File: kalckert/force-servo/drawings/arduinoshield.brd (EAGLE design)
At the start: 100 x 80 mm, 24 parts, among them IC1 MCP604P, IC3 7806T

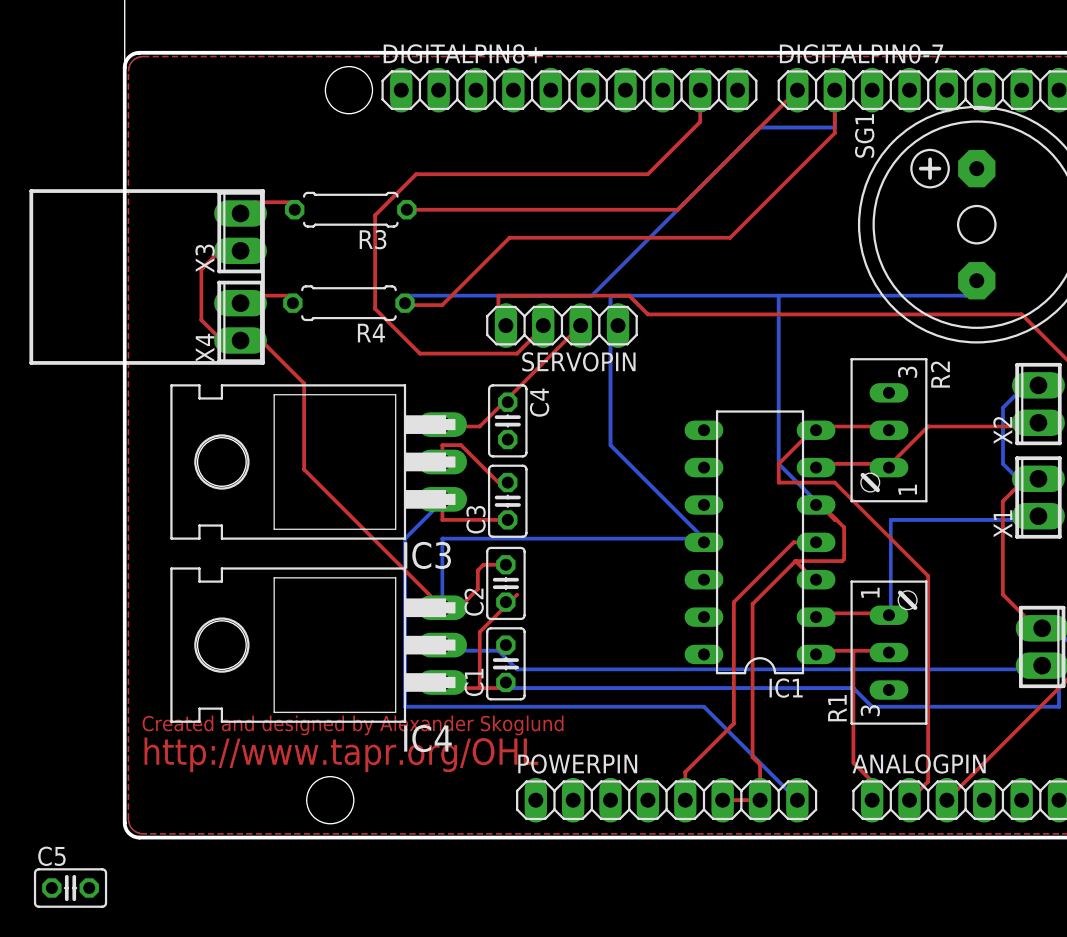
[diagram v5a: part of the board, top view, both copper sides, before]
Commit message: Added a calibration sequence in the arduino program.
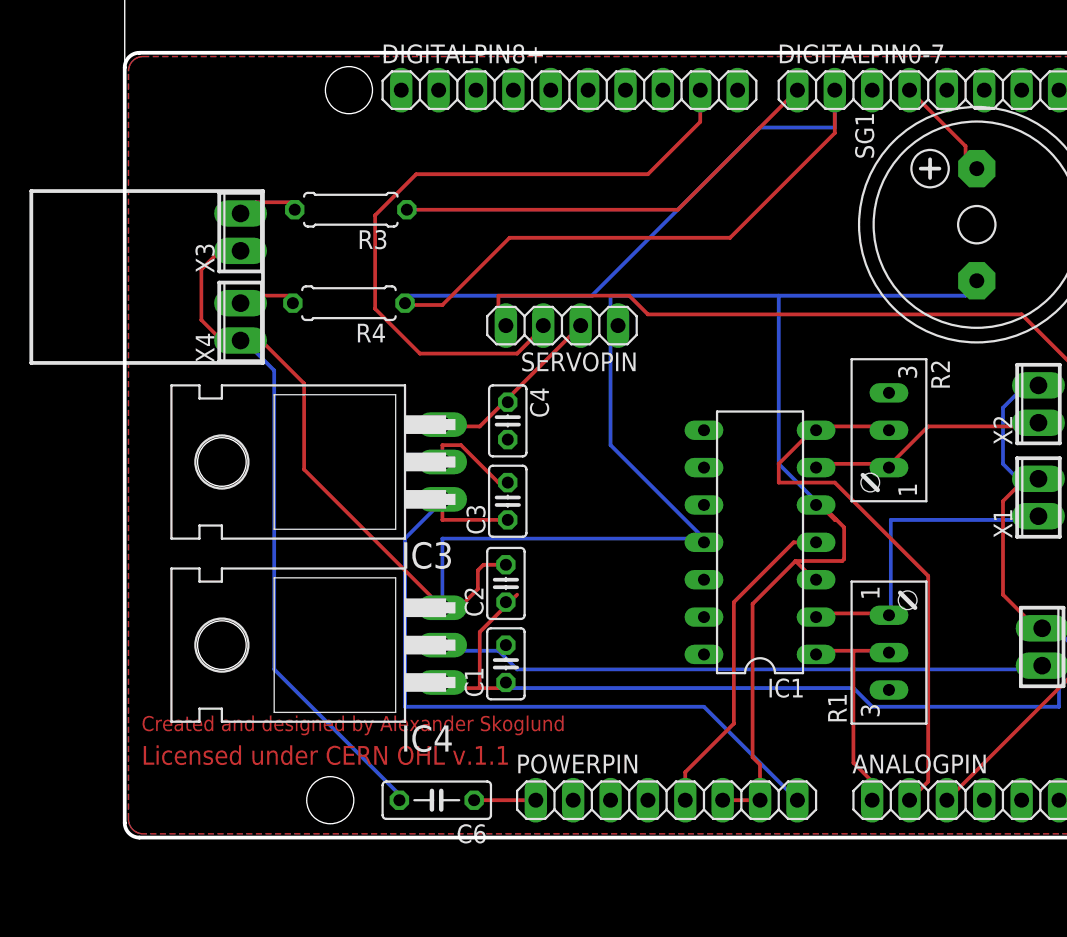
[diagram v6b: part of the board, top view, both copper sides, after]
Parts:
- removed C5: 10uF, resistor:C025-025X050
- added C6: 10uF, resistor:C050-025X075
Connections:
- net GND: now also C6.2; no longer C5.2
- net RESET: now also C6.1; no longer C5.1
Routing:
- net GND: track 156.7 -> 193.0 mm
- net BUZZER: track 0.00 -> 7.46 mm
- net RESET: track 0.00 -> 4.19 mm
- net N$3: track 6.13 -> 6.77 mm
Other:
- board text added: "Licensed under CERN OHL v.1.1"
- board text removed: "http://www.tapr.org/OHL"
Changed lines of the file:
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@@
 <wire x1="9.398" y1="32.258" x2="-6.35" y2="32.258" width="0.254" layer="21"/>
 <wire x1="-6.35" y1="32.258" x2="-6.35" y2="43.942" width="0.254" layer="21"/>
-<text x="1.143" y="4.953" size="1.778" layer="1">http://www.tapr.org/OHL</text>
+<text x="1.143" y="4.953" size="1.27" layer="1">Licensed under CERN OHL v.1.1</text>
 <text x="1.143" y="7.239" size="1.016" layer="1">Created and designed by Alexander Skoglund</text>
 </plain>
@@
 <attribute name="OC_FARNELL" value="unknown" x="80.137" y="59.69" size="1.778" layer="27" rot="R90" display="off"/>
 </element>
-<element name="C5" library="resistor" package="C025-025X050" value="10uF" x="-3.683" y="-3.429"/>
+<element name="C6" library="resistor" package="C050-025X075" value="10uF" x="21.209" y="2.54" rot="R180"/>
 </elements>
 <signals>
@@
 <wire x1="39.37" y1="20.32" x2="39.37" y2="20.066" width="0.254" layer="16"/>
 <wire x1="21.59" y1="15.24" x2="21.59" y2="15.621" width="0.254" layer="16"/>
-<contactref element="C5" pad="2"/>
-<wire x1="-2.413" y1="-3.429" x2="21.59" y2="15.24" width="0" layer="19" extent="16-16"/>
+<contactref element="C6" pad="2"/>
+<wire x1="10.16" y1="11.43" x2="19.05" y2="2.54" width="0.254" layer="16"/>
+<wire x1="10.16" y1="31.75" x2="10.16" y2="11.43" width="0.254" layer="16"/>
+<wire x1="8.89" y1="33.02" x2="10.16" y2="31.75" width="0.254" layer="16"/>
+<wire x1="19.05" y1="2.54" x2="18.669" y2="2.54" width="0.254" layer="16"/>
+<wire x1="8.89" y1="33.02" x2="7.874" y2="33.782" width="0.254" layer="16"/>
 </signal>
 <signal name="VCCSERVO">
@@
 <contactref element="SG1" pad="+"/>
 <contactref element="DIGITALPIN0-7" pad="4"/>
-<wire x1="57.912" y1="45.466" x2="53.34" y2="50.8" width="0" layer="19" extent="1-1"/>
+<wire x1="57.15" y1="46.99" x2="53.34" y2="50.8" width="0.254" layer="1"/>
+<wire x1="57.15" y1="45.72" x2="57.15" y2="46.99" width="0.254" layer="1"/>
+<wire x1="57.15" y1="45.72" x2="57.912" y2="45.466" width="0.254" layer="1"/>
 </signal>
 <signal name="VIN">
@@
 <wire x1="39.37" y1="8.89" x2="45.72" y2="2.54" width="0.254" layer="16"/>
 <wire x1="19.05" y1="8.89" x2="39.37" y2="8.89" width="0.254" layer="16"/>
-<wire x1="19.05" y1="20.32" x2="19.05" y2="8.89" width="0.254" layer="16"/>
 <wire x1="21.59" y1="22.86" x2="19.05" y2="20.32" width="0.254" layer="16"/>
 <wire x1="21.59" y1="22.86" x2="21.59" y2="22.987" width="0.254" layer="16"/>
+<wire x1="19.05" y1="8.89" x2="19.05" y2="20.32" width="0.254" layer="16"/>
 </signal>
 <signal name="N$3">
@@
 <contactref element="C3" pad="2"/>
 <contactref element="C4" pad="2"/>
+<wire x1="25.4" y1="24.13" x2="26.035" y2="24.13" width="0.254" layer="1"/>
 <wire x1="26.035" y1="24.13" x2="26.035" y2="27.051" width="0" layer="19" extent="1-1"/>
-<wire x1="25.4" y1="24.13" x2="26.035" y2="24.13" width="0" layer="19" extent="1-1"/>
 </signal>
 <signal name="LED_GREEN">
@@
 <signal name="RESET">
 <contactref element="POWERPIN" pad="1"/>
-<contactref element="C5" pad="1"/>
-<wire x1="-4.953" y1="-3.429" x2="27.94" y2="2.54" width="0" layer="19" extent="1-1"/>
+<contactref element="C6" pad="1"/>
+<wire x1="27.94" y1="2.54" x2="23.749" y2="2.54" width="0.254" layer="1"/>
 </signal>
 </signals>
